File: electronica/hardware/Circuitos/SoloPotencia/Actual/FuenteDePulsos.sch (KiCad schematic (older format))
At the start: 42 parts, among them J1 Conn_01x03, J2 Conn_01x05, J5 Agujero, J6 Agujero, J7 Agujero, J8 Agujero, Q1 2N3906, Q2 2N3906, Q3 2N3904, Q4 2N3904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

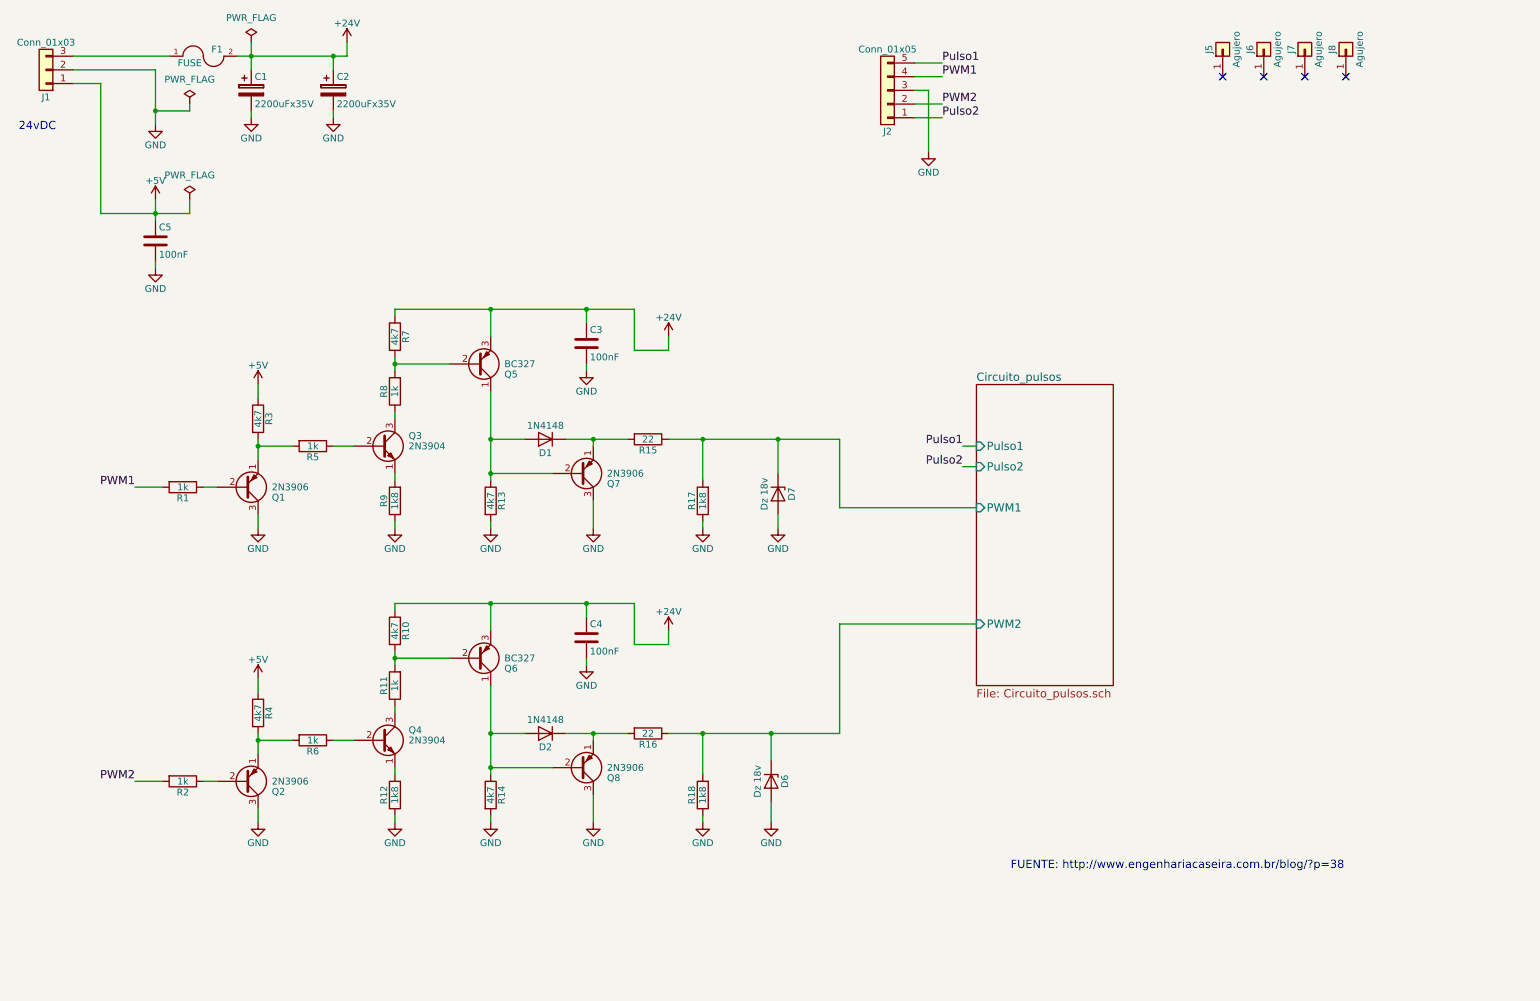
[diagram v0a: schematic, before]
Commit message: Se agregaron mediciones a la placa de potencia. Las mediciones con un informe se encuentran en ProcesoPTH/documentacion/MedicionesFuenteDePulsos
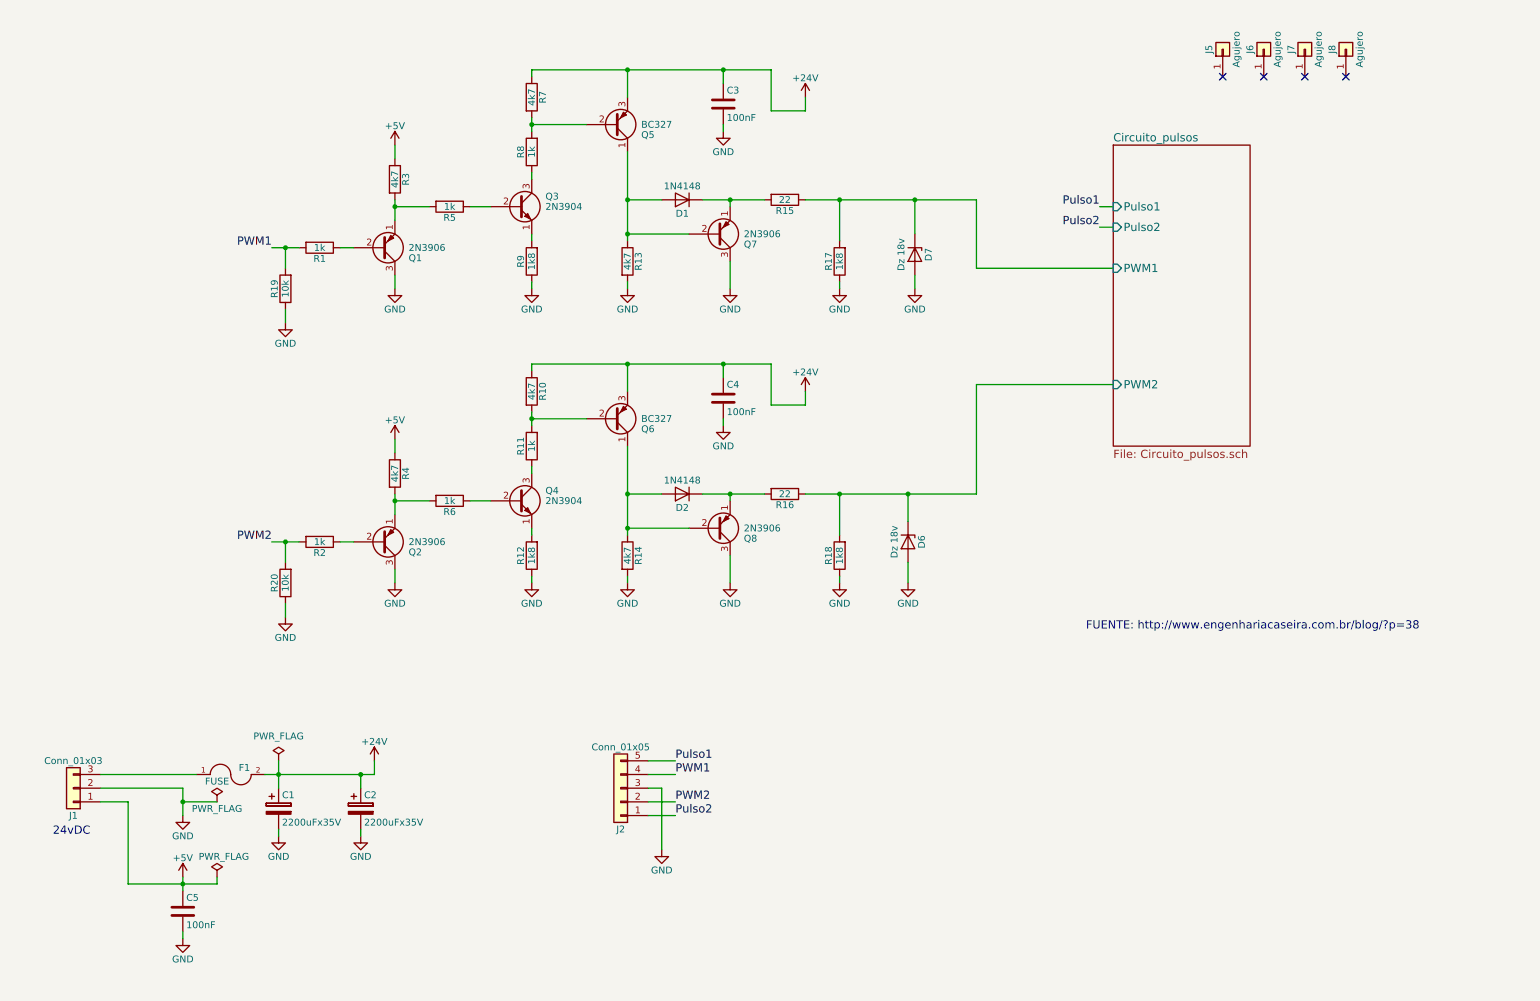
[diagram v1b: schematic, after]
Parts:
- added R19, R20: 10k, Resistors_THT:R_Axial_DIN0207_L6.3mm_D2.5mm_P7.62mm_Horizontal, symbol FuenteDePulsos-rescue:R
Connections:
- net GND: now also R19.1, R20.1
- net PWM1: now also R19.2
- net PWM2: now also R20.2
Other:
- moved on the sheet: C1, C2, C3, C4, C5, D1, D2, D6, D7, F1, J1, J2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

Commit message: Se agregaron mediciones con el nuevo driver para el transistor PMOS
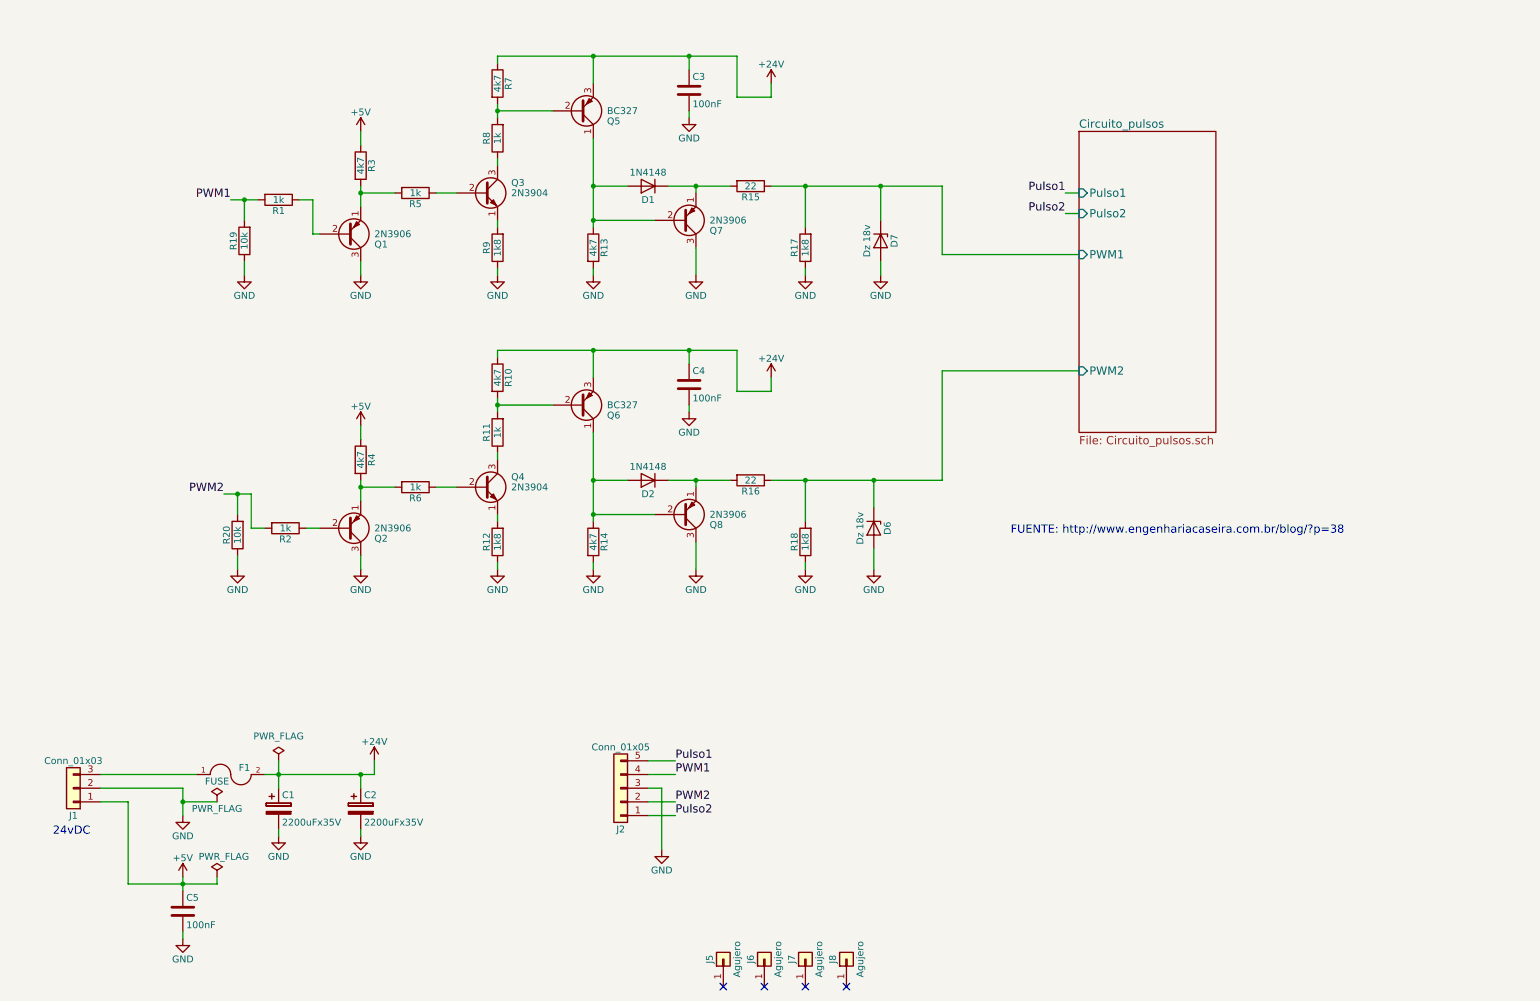
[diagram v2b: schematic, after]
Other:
- moved on the sheet: C3, C4, D1, D2, D6, D7, J5, J6, J7, J8, Q1, Q2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
